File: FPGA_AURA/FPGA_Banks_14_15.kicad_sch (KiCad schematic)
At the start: 1 part, among them U1 XC7A35T-2FTG256C

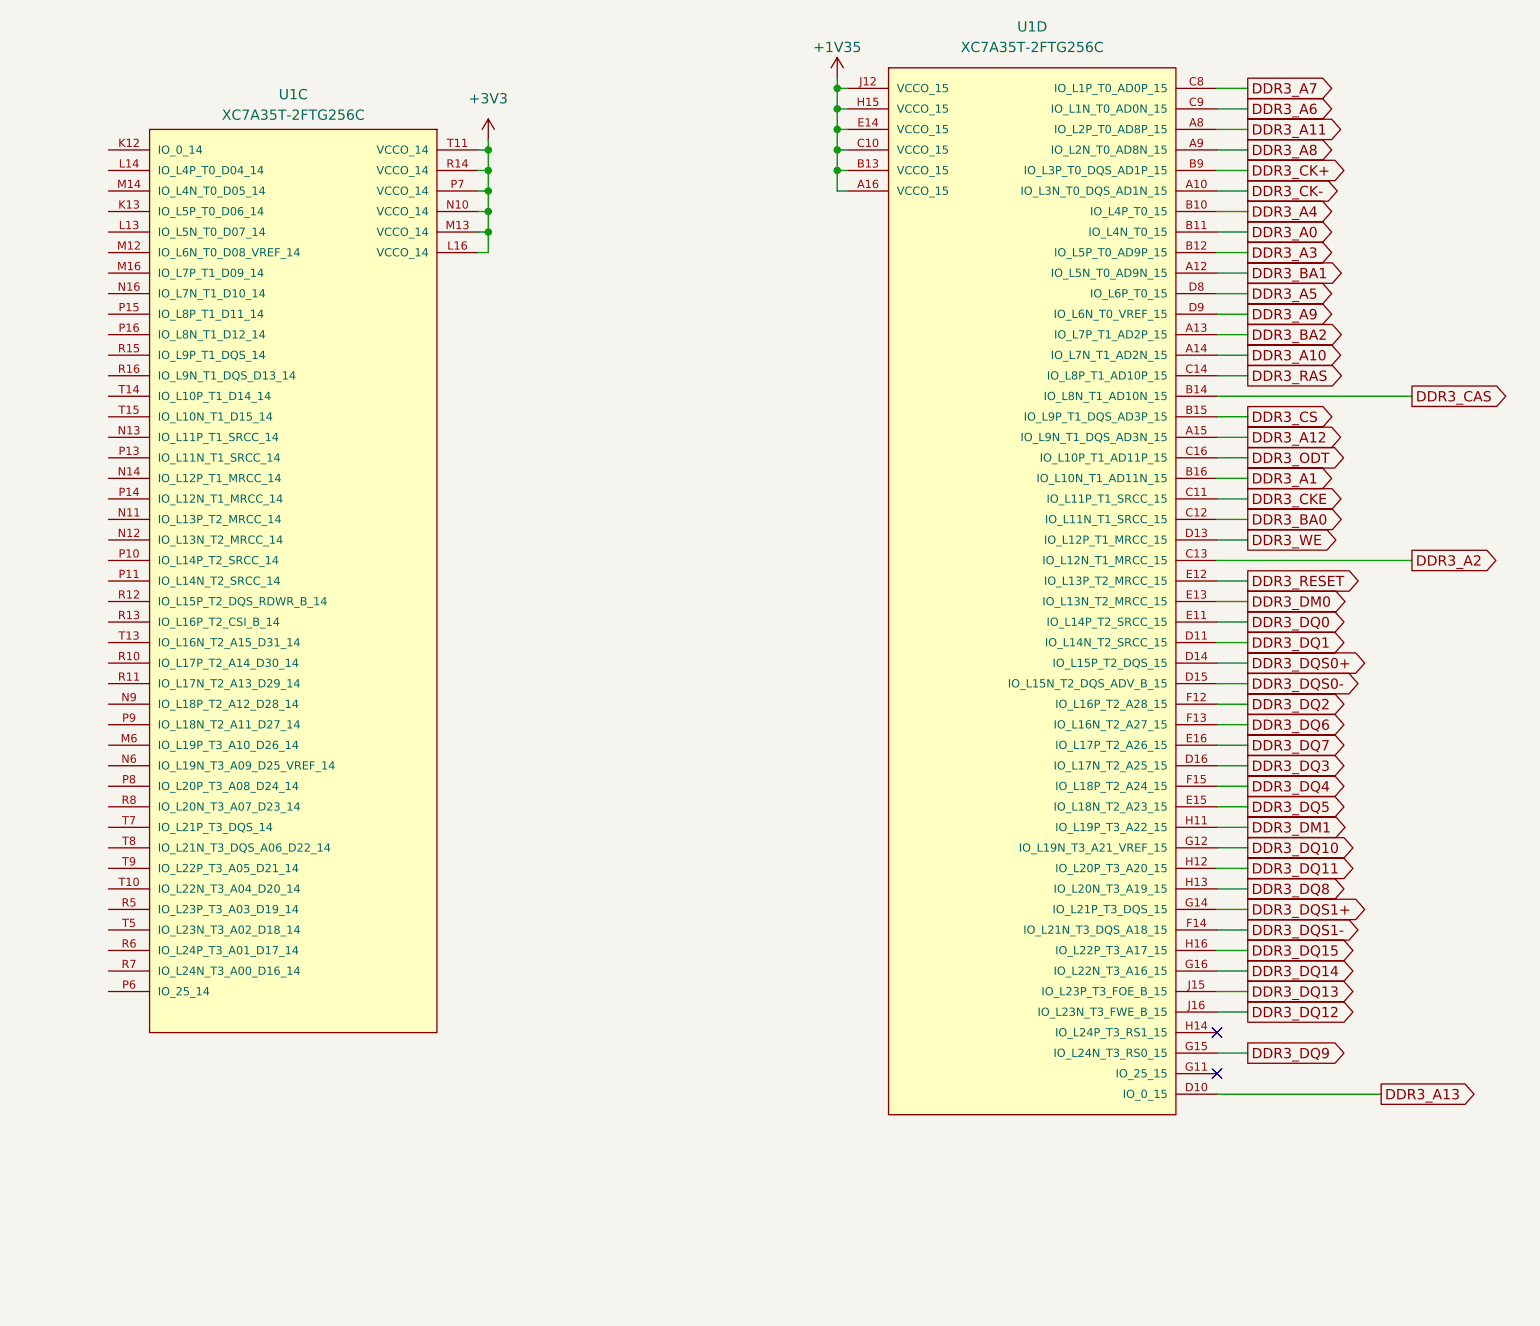
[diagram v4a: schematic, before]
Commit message: Changing stackup to 10 layers and connectors change
Development has been slow due to SI concerns with 8 layers so changing the layer count to 10 will simplify design. The picoblade/SD connector(s) are large and not high speed, so a high speed mezzanine will be used to go to a daughter board with the picoblade connectors and SD card, or other devices/protocols e.g. ADCs, COAX, IMUs, etc.
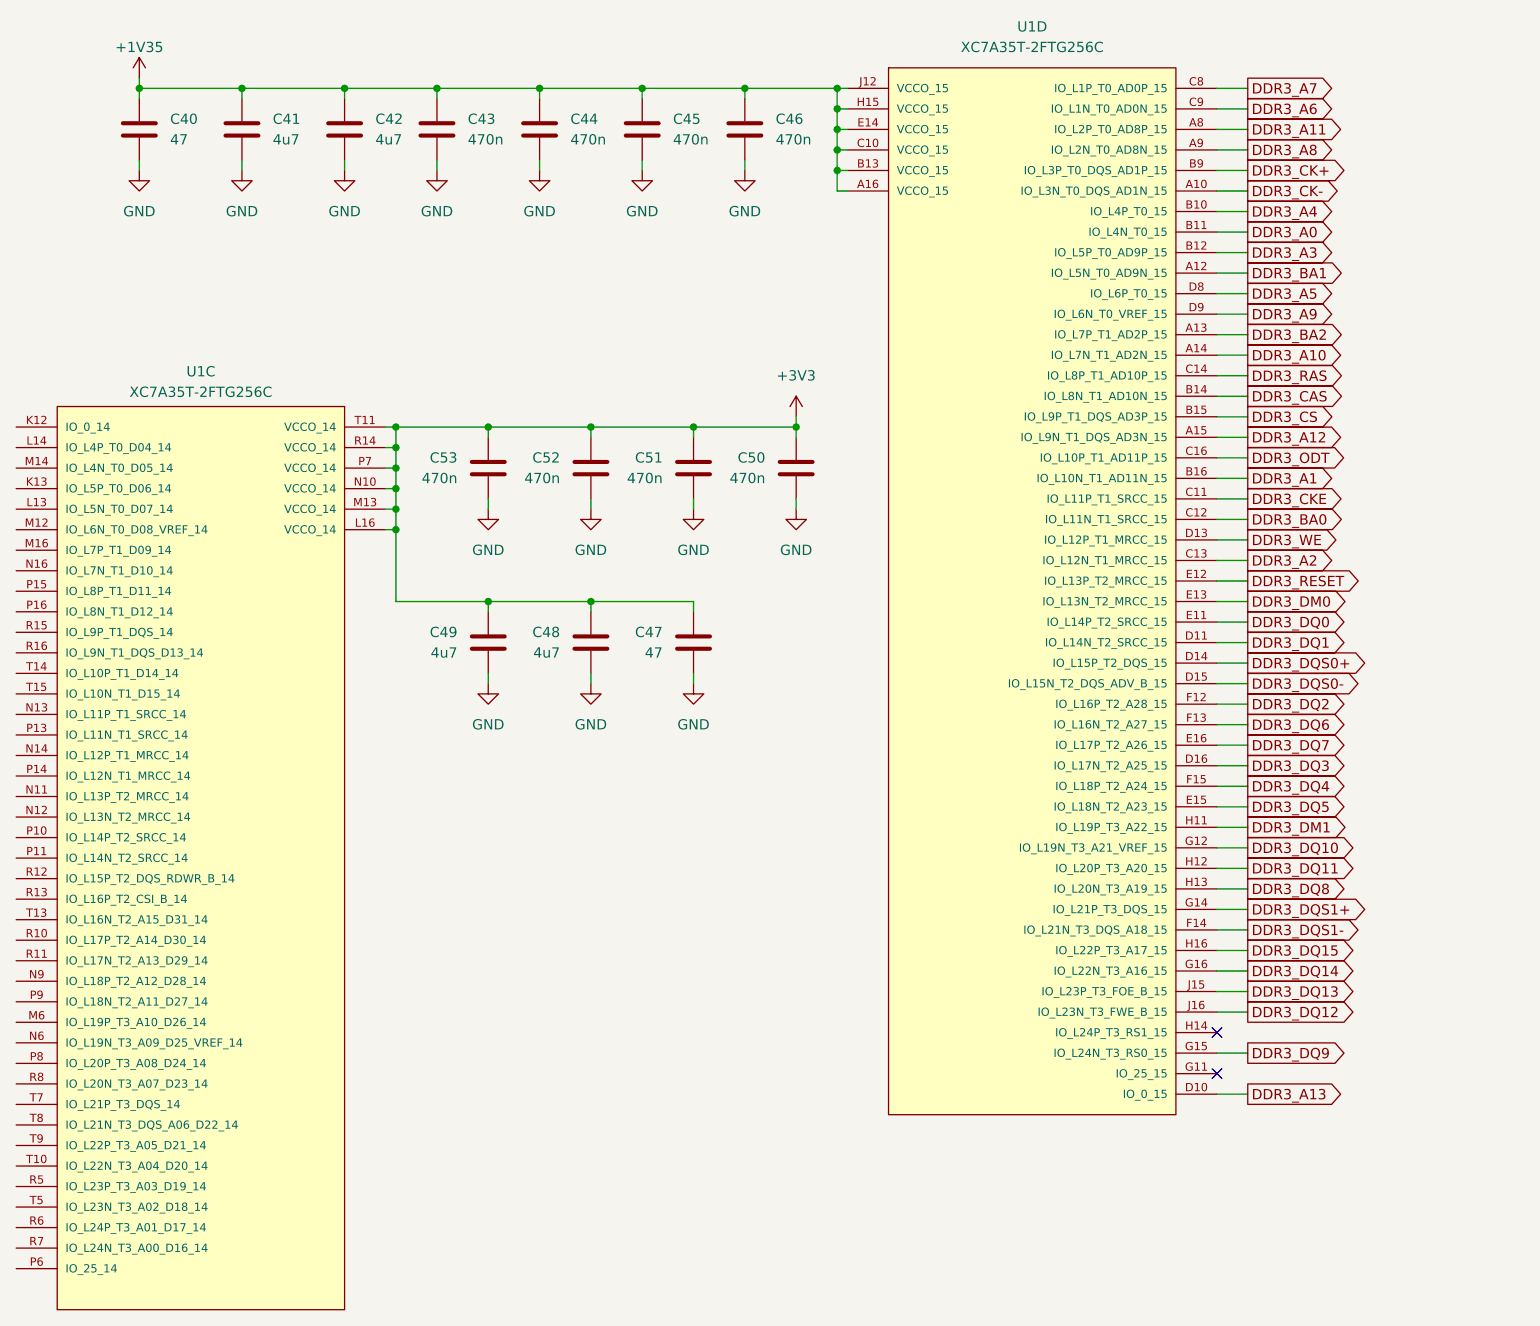
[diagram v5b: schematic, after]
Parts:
- added C40, C47: 47, Capacitor_SMD:C_0603_1608Metric, symbol Device:C
- added C41, C42, C48, C49: 4u7, Capacitor_SMD:C_0603_1608Metric, symbol Device:C
- added C43, C44, C45, C46, C50, C51, C52, C53: 470n, Capacitor_SMD:C_0402_1005Metric, symbol Device:C
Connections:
- net +1V35: now also C40.1, C41.1, C42.1, C43.1, C44.1, C45.1, C46.1
- net +3V3: now also C47.1, C48.1, C49.1, C50.1, C51.1, C52.1, C53.1
- new net GND: C40.2, C41.2, C42.2, C43.2, C44.2, C45.2, C46.2, C47.2, C48.2, C49.2, C50.2, C51.2, C52.2, C53.2
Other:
- moved on the sheet: U1C
